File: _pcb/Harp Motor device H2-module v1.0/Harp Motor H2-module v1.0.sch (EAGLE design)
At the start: 52 parts, among them IC1 FT232RL, IC3 LP5907MFX-3.3, IC7 USBLC6-2SC6, IC8 ATXMEGA32A4U, J1 BNCPTH, J2 BNCPTH, J3 POWER_JACK, X1 22-23-2051, X15 Main_plug, X2 22-23-2051, X3 USB_MINI_B, X4 1x4 case, X5 1x3 case, X6 CLCK_JACK, X7 1x4 case, X8 22-23-2021

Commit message: VestibularVR H1BOM updates & Lick Sensor step on
- VestibularVR H1
. component ref updated
. BOM file updated

- Lick Sensor module v1.0
. still only on schematic design
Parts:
- removed J1, J2: BNCPTH, SparkFun-Connectors:BNCPTH
- removed J3: POWER_JACK, SparkFun-Connectors:POWER_JACK
- removed X15: Main_plug, con-weidmueller-sl35:90G-5
- removed X5: 1x3 case, con-molex:22-23-2031
- removed X8: 22-23-2021, con-molex:22-23-2021
- added C1, C14, C15, C16, C17: 100nF, rcl:C-EUC0402K
- added C23, C24: 4.7uF, rcl:C-EUC0603
- added CLKIN: CLCK_JACK, harp input expander:STEREO_JACK
- added HARP: Harp_Intrfc, con-weidmueller-sl35:90G-5
- added IC2, IC4, IC5: 74VHC1GT126DT1G, VestibularVR H1-module v1.0:74LVC1G07DBV
- added IC9: TLV70033DDCR, harp input expander:TLV700XX
- added R1: 330R, rcl:R-US_R0402
- added R11: DNI, rcl:R-US_R0402
- added R12, R13, R2, R4, R6, R7, R8: 10k, rcl:R-US_R0402
- added R5: 10R, rcl:R-US_R0402
- added R9: 1M, rcl:R-US_R0402
- added T1, T2, T3: DMG1012UW??, VestibularVR H1-module v1.0:DMG1012UW-7
- R10: value 330R -> 0R; device rcl:R-EU_R0402 -> rcl:R-US_R0402; MPN RC0402FR-07330RL -> RC0402JR-070RL; OEPS OEPS020037 -> OEPS020001
- R18, R34: DIGIKEY_PN 541-3959-1-ND -> 541-10.0KLDKR-ND
- X1: value 22-23-2051 -> USB_MINI_B; device con-molex:22-23-2051 -> VestibularVR H1-module v1.0:USB_MINI_B; MPN (none) -> UX60-MB-5S8; OEPS (none) -> OEPS070021
- X2: value 22-23-2051 -> Rot_Encoder
- X3: value USB_MINI_B -> EMRG_BUTT_IN_NO; device VestibularVR H1-module v1.0:USB_MINI_B -> con-molex:22-23-2021; MPN UX60-MB-5S8 -> (none); OEPS OEPS070021 -> (none)
- X4: value 1x4 case -> Hall_Effect; device con-molex:22-23-2041 -> con-molex:22-23-2031; MPN 282834-4 Digikey A98335-ND -> 282834-3; OEPS OEPS07 xxx1 -> OEPS070035
- X6: value CLCK_JACK -> BNCPTH; device harp input expander:STEREO_JACK -> SparkFun-Connectors:BNCPTH; MPN 35RASMT2BHNTRX -> (none); NOTES - -> (none); TYPE SMD -> (none)
- X7: value 1x4 case -> STEP_MOTOR; device con-molex:22-23-2041 -> con-molex:22-23-2051; MF - -> (none); MPN 282834-4 Digikey A98335-ND -> (none); OEPS OEPS07 xxx1 -> (none)
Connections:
- removed net N$4: X1-5.S, X2-5.S, X4-4.S
- new net A_PHASE: IC4.A, X2-3.S
- new net B_PHASE: IC5.A, X2-4.S
- new net CLOCK_IN: CLKIN.4, IC8.PB1/ADC9, R2.1
- new net EMERGENCY_INPUT: IC8.PB0/ADC8/AREF, R8.1, X3-1.S
- new net HALL_EFFCT_IN: IC2.A, X4-2.S
- new net LICK_PORT_1: R9.2
- new net N$103: CLKIN.1, R2.2, R5.2
- new net N$104: C24.1, IC9.OUT, R5.1
- new net N$5: C1.1, IC2.VCC, R10.2, R11.2, X4-3.S
- new net STEP_DIRECTION: T1.D, X7-3.S
- new net STEP_ENABLE: T2.D, X7-4.S
- new net STEP_PULSE: T3.D, X7-2.S
- new net U_A_PHASE: IC4.Y, IC8.PC4/OC1A/!SS
- new net U_B_PHASE: IC5.Y, IC8.PC3/OC0D/TXD0
- new net U_HALL_EFFCT_IN: IC2.Y, IC8.PA0/ADC0/AREF
- new net U_STEP_DIRECTION: IC8.PC6/MISO/RXD1, R12.2, T1.G
- new net U_STEP_ENABLE: IC8.PC5/OC1B/MOSI/XCK1, R6.2, T2.G
- new net U_STEP_PULSE: IC8.PC7/SCK/TXD1/CLKO/EVO, R13.2, T3.G
- new net V+: R8.2
- net +12V: now also HARP.1; no longer X15.1
- net +3V3: now also R10.1; no longer X5-3.S
- net +5V: now also C14.1, C17.1, C23.1, IC4.VCC, IC5.VCC, IC9.EN, IC9.IN, R11.1, X2-1.S, X7-1.S
- net GND: now also C1.2, C14.2, C15.2, C16.2, C17.2, C23.2, C24.2, CLKIN.5, HARP.5, IC2.GND, IC4.GND, IC5.GND, IC9.GND, R1.1, R12.1, R13.1, R4.1, R6.1, R7.1, R9.1, T1.S, T2.S, T3.S, X1.5, X2-5.S, X3-2.S, X6.GND, X7-5.S; no longer R10.1, X1-1.S, X15.5, X2-1.S, X3.5, X5-1.S, X6.5
- net HARP_H1_CLOCK_IN: now also HARP.4; no longer X1-2.S
- net HARP_H1_RX: now also HARP.3; no longer X1-3.S
- net HARP_H1_TX: now also HARP.2; no longer X1-4.S
- net N$1: now also X1.P$2; no longer X3.P$2
- net N$15: now also X1.P$3; no longer X3.P$3
- net N$2: now also X1.2; no longer X3.2
- net N$3: now also X1.3; no longer X3.3
- net N$9: now also R1.2; no longer R10.2
- net USB_POWER: now also X1.1; no longer X3.1
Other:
- note added: "Emergency Button NO in"
- note added: "H1 Harp interface InOut"
- note added: "Hall Effect sensor in"
- note added: "harp Clock in"
- note added: "in Stage rotation signal BNC plug: (be sure about)"
- note added: "main USB"
- note added: "out step motor control"
- note removed: "5V~24V inputs (??)"
- note removed: "CHECK VOLTAGE LEVEL OUTPUT!!!"
- note removed: "InOut H1 Harp interface"
- note removed: "Main Plug"
- note removed: "in Clock input"
- note removed: "in Emergency Button"
- note removed: "in Hall Effect sensor"
- note removed: "in jumpers to setup/test open or closed loop control??"
- note removed: "in sphere rotation signal"
- note removed: "in stage rotation signal ?? 2 signals??"
- note removed: "level translatioon 5V -> 3V3"
- note removed: "level translatioon 5V~24V -> 3V3"
- note removed: "out step motor driver"
- note removed: "to u; PullDown"
- moved on the sheet: C10, C11, C12, C13, C2, C25, C26, C27, C28, C29, C3, C4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

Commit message: Harp Motor device H2-module v1.0 - Schematic step on
Harp Motor device H2-module v1.0 - Schematic step on
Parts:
- removed C15, C16: 100nF, rcl:C-EUC0402K
- removed HARP: Harp_Intrfc, con-weidmueller-sl35:90G-5
- removed R10: 0R, rcl:R-US_R0402
- removed R11: DNI, rcl:R-US_R0402
- removed R4, R7: 10k, rcl:R-US_R0402
- removed R9: 1M, rcl:R-US_R0402
- added H2_MAIN_PLUG: be sure about plug type, Harp Motor H2-module v1.0:90G-5
- added IC6: 74AHC1G125DBV, Harp Motor H2-module v1.0:74AHC1G125DBV
- added PWR1: DC_JACK2.1MM, harp camera controller:DC_JACK2.1MM
- C1, C12, C13, C14, C17, C2, C25, C26, C27, C28, C29, C3, C4, C5, C6, C7, C9: device rcl:C-EUC0402K -> Harp Motor H2-module v1.0:C-EUC0402K
- C10, C11: device rcl:C-EUC0603K -> Harp Motor H2-module v1.0:C-EUC0603K
- C8: device rcl:C-EUC0603 -> Harp Motor H2-module v1.0:C-EUC0603
- D4: device diode:BAT54 -> Harp Motor H2-module v1.0:BAT54
- L1, L2: device rcl:R-EU_R0603 -> Harp Motor H2-module v1.0:R-EU_R0603
- R1, R12, R13, R18, R2, R3, R34, R5, R6, R8: device rcl:R-US_R0402 -> Harp Motor H2-module v1.0:R-US_R0402
- STATE: device led:LEDCHIP-LED0603 -> Harp Motor H2-module v1.0:LEDCHIP-LED0603
- SV2: device Connector:PINHD-2X3 -> Harp Motor H2-module v1.0:PINHD-2X3
- TP1, TP10, TP11, TP13: device testpad:TPB1,27 -> Harp Motor H2-module v1.0:TPB1,27
- TP4, TP5, TP6, TP8, TP9: device testpad:TPSQTP11R -> Harp Motor H2-module v1.0:TPSQTP11R
- X2, X7: device con-molex:22-23-2051 -> Harp Motor H2-module v1.0:22-23-2051
- X3: device con-molex:22-23-2021 -> Harp Motor H2-module v1.0:22-23-2021
- X4: device con-molex:22-23-2031 -> Harp Motor H2-module v1.0:22-23-2031
- X6: device SparkFun-Connectors:BNCPTH -> Harp Motor H2-module v1.0:BNCPTH
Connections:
- net A_PHASE renamed ENCODER_A_PHASE
- net B_PHASE renamed ENCODER_B_PHASE
- net U_A_PHASE renamed U_ENCODER_A_PHASE
- net U_B_PHASE renamed U_ENCODER_B_PHASE
- removed net +12V: D4.C, HARP.1
- removed net HARP_H1_CLOCK_IN: HARP.4
- removed net HARP_H1_RX: HARP.3
- removed net HARP_H1_TX: HARP.2
- removed net LICK_PORT_1: R9.2
- removed net N$5: C1.1, IC2.VCC, R10.2, R11.2, X4-3.S
- removed net N$6: D4.A
- new net HARP_H2_CLOCK_IN: H2_MAIN_PLUG.4, IC8.D-/RXD1/MISO/PD6
- new net HARP_H2_RX: H2_MAIN_PLUG.3, IC8.OCB1/XCK1/MOSI/PD5
- new net HARP_H2_TX: H2_MAIN_PLUG.2, IC8.OC1A/!SS!/PD4
- new net N$4: X7-1.S
- new net VDD: H2_MAIN_PLUG.1, PWR1.1
- net +3V3: now also C1.1, IC2.VCC, X4-2.S; no longer R10.1
- net +5V: no longer R11.1, X7-1.S
- net GND: now also H2_MAIN_PLUG.5, PWR1.2, PWR1.3, X4-3.S; no longer C15.2, C16.2, HARP.5, R4.1, R7.1, R9.1, X4-1.S, X6.GND
- net HALL_EFFCT_IN: now also X4-1.S; no longer X4-2.S
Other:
- note added: "BNCs output: connected to two Teensy DAC Stage rotation signal (be sure about)"
- note added: "Camera Controller - Clock_IN: PC2 H1 tb mesmo pino?? - interrupst (?): PC0 PD0 - analog IN: ?? - camera Strobes (Interrupts?): CAM0: PA0=Strobe & PA1=PullUp CAM1: PD6=PullUp & PD7=Strobe"
- note added: "H2 Harp External Power Input - straight to H1 module"
- note added: "H2 Harp main IO plug"
- note added: "USB"
- note added: "V AREV para 3V3 ?!? e Ain para A1"
- note added: "check ferrite case"
- note added: "check pinout not as in abstarct draw"
- note added: "confirmar encoder A & B phase: OC0A & OC0B"
- note added: "connection to Rotary Joint = H1 module"
- note added: "input Emergency Button NO"
- note added: "input Hall Effect home sensor"
- note added: "input harp Clock"
- note added: "input missing?? Treadmill Motion?? what have to do about it?"
- note added: "input rotary encoder"
- note added: "open drain output!! R pull-up out"
- note added: "output step motor control"
- note added: "pinout order: same as sensor"
- note added: "power rail: - Vcc to stepper drive controller optos - DM542 stepper drive controller Vcc: = 5V~24V >> output voltage here can be 5V - Imax = ???"
- note added: "rail de 5V ???? saida para o micro!!!"
- note added: "sensor: WINGONEER JT0701"
- note added: "use the other buffer with EN pin?? that way both buffers can be used"
- note removed: "Emergency Button NO in"
- note removed: "H1 Harp interface InOut"
- note removed: "Hall Effect sensor in"
- note removed: "harp Clock in"
- note removed: "in Stage rotation signal BNC plug: (be sure about)"
- note removed: "in rotary encoder"
- note removed: "main USB"
- note removed: "out step motor control"
- moved on the sheet: C1, C10, C11, C12, C13, C14, C17, C2, C23, C24, C25, C26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

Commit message: Harp Motor device H2-module v1.0 - design proceeding
Harp Motor device H2-module v1.0 - design proceeding
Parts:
- removed IC2, IC4, IC5: 74VHC1GT126DT1G, VestibularVR H1-module v1.0:74LVC1G07DBV
- removed IC6: 74AHC1G125DBV, Harp Motor H2-module v1.0:74AHC1G125DBV
- removed X6: BNCPTH, Harp Motor H2-module v1.0:BNCPTH
- added IC11, IC12, IC13: 74LVC1G125DBV, Harp Motor H2-module v1.0:74LVC1G125DBV
- added R4: 0R, Harp Motor H2-module v1.0:R-US_R0402
- added R7: 10k, Harp Motor H2-module v1.0:R-US_R0402
- R13: value 10k -> DNI; DIGIKEY_PN 541-10.0KLDKR-ND -> -; MPN CRCW040210K0FKED -> -; OEPS OEPS020030 -> -
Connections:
- removed net N$4: X7-1.S
- removed net V+: R8.2
- new net AREF: IC8.PA0/ADC0/AREF, R4.1, R7.2
- net +3V3: now also C14.1, C17.1, IC11.VCC, IC12.VCC, IC13.VCC; no longer IC2.VCC
- net +3V3_U: now also R4.2, R8.2
- net +5V: now also X7-1.S; no longer C14.1, C17.1, IC4.VCC, IC5.VCC
- net ENCODER_A_PHASE: now also IC11.I; no longer IC4.A
- net ENCODER_B_PHASE: now also IC12.I; no longer IC5.A
- net GND: now also IC11.GND, IC11.OE, IC12.GND, IC12.OE, IC13.GND, IC13.OE, R7.1; no longer IC2.GND, IC4.GND, IC5.GND
- net HALL_EFFCT_IN: now also IC13.I; no longer IC2.A
- net U_ENCODER_A_PHASE: now also IC11.O; no longer IC4.Y
- net U_ENCODER_B_PHASE: now also IC12.O; no longer IC5.Y
- net U_HALL_EFFCT_IN: now also IC13.O, IC8.PA1/ADC1; no longer IC2.Y, IC8.PA0/ADC0/AREF
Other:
- note added: "BNCs output: needed?? connected to two Teensy DAC Stage rotation signal ?? (be sure about) maybe only auxiliary IO.."
- note removed: "BNCs output: connected to two Teensy DAC Stage rotation signal (be sure about)"
- note removed: "V AREV para 3V3 ?!? e Ain para A1"
- note removed: "open drain output!! R pull-up out"
- note removed: "rail de 5V ???? saida para o micro!!!"
- note removed: "use the other buffer with EN pin?? that way both buffers can be used"
- moved on the sheet: C1, C14, C17

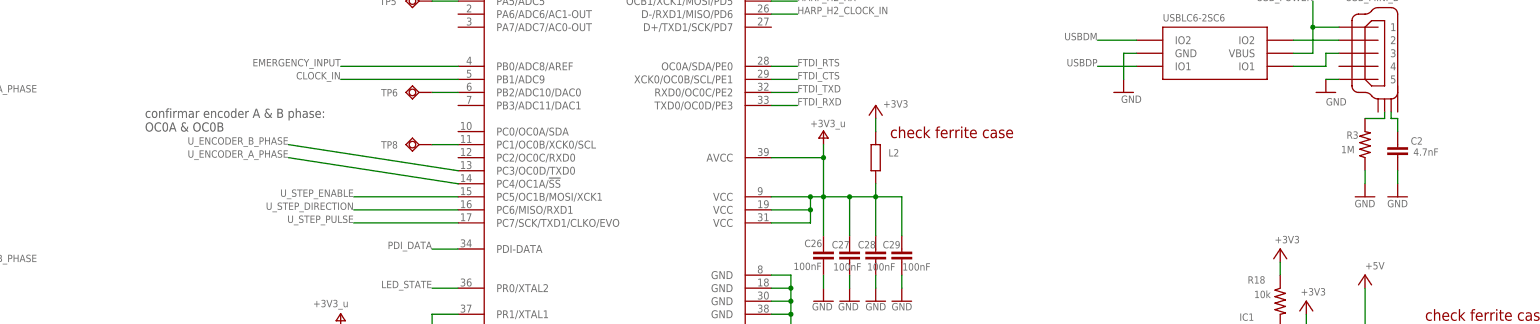
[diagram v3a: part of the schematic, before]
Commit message: Harp Motor device H2-module v1.0 - 1st 'finished' version
Harp Motor device H2-module v1.0 - 1st 'finished' version
- missing:
   . some schm & pcb review with Filipe
   . components order codes & BOM
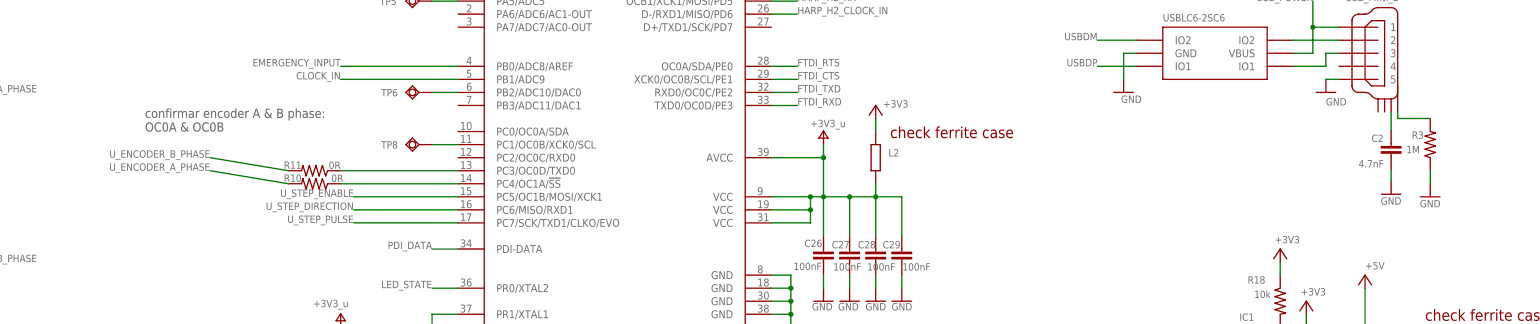
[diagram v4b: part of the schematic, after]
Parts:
- added R10, R11: 0R, Harp Motor H2-module v1.0:R-US_R0402
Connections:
- new net N$59: IC8.PC4/OC1A/!SS, R10.1
- new net N$60: IC8.PC3/OC0D/TXD0, R11.1
- net N$1: now also X1.P$4; no longer X1.P$2
- net U_ENCODER_A_PHASE: now also R10.2; no longer IC8.PC4/OC1A/!SS
- net U_ENCODER_B_PHASE: now also R11.2; no longer IC8.PC3/OC0D/TXD0
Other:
- moved on the sheet: C2, R3
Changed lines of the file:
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@@
 <attribute name="TYPE" value="SMD"/>
+</part>
+<part name="R10" library="Harp Motor H2-module v1.0" deviceset="R-US_" device="R0402" value="0R">
+<attribute name="DIGIKEY_PN" value="o 0R"/>
+<attribute name="MPN" value="MPN ??"/>
+<attribute name="OEPS" value="OEPS?? q codigo"/>
+</part>
+<part name="R11" library="Harp Motor H2-module v1.0" deviceset="R-US_" device="R0402" value="0R">
+<attribute name="DIGIKEY_PN" value="o 0R"/>
+<attribute name="MPN" value="MPN ??"/>
+<attribute name="OEPS" value="OEPS?? q codigo"/>
 </part>
 </parts>
@@
 <attribute name="OEPS" x="358.14" y="101.6" size="1.778" layer="96" rot="MR180" display="off"/>
 </instance>
-<instance part="C2" gate="G$1" x="358.14" y="139.7" smashed="yes">
-<attribute name="NAME" x="360.68" y="139.7" size="1.4224" layer="95" font="vector" ratio="12"/>
-<attribute name="VALUE" x="361.188" y="137.541" size="1.4224" layer="96" font="vector" ratio="12"/>
-<attribute name="MPN" x="358.14" y="139.7" size="1.778" layer="96" display="off"/>
-<attribute name="OEPS" x="358.14" y="139.7" size="1.778" layer="96" display="off"/>
+<instance part="C2" gate="G$1" x="356.87" y="139.954" smashed="yes">
+<attribute name="NAME" x="353.06" y="140.208" size="1.4224" layer="95" font="vector" ratio="12"/>
+<attribute name="VALUE" x="350.52" y="135.255" size="1.4224" layer="96" font="vector" ratio="12"/>
+<attribute name="MPN" x="356.87" y="139.954" size="1.778" layer="96" display="off"/>
+<attribute name="OEPS" x="356.87" y="139.954" size="1.778" layer="96" display="off"/>
 </instance>
 <instance part="GND33" gate="1" x="345.44" y="71.12" smashed="yes">
@@
 <attribute name="VALUE" x="304.292" y="147.828" size="1.4224" layer="96" font="vector" ratio="12"/>
 </instance>
-<instance part="R3" gate="G$1" x="351.79" y="139.7" smashed="yes" rot="R90">
-<attribute name="NAME" x="350.52" y="142.2654" size="1.4224" layer="95" font="vector" ratio="12" rot="R180"/>
-<attribute name="VALUE" x="349.758" y="139.446" size="1.4224" layer="96" font="vector" ratio="12" rot="R180"/>
-<attribute name="MPN" x="351.79" y="139.7" size="1.778" layer="96" rot="R90" display="off"/>
-<attribute name="OEPS" x="351.79" y="139.7" size="1.778" layer="96" rot="R90" display="off"/>
-<attribute name="DIGIKEY_PN" x="351.79" y="139.7" size="1.778" layer="96" rot="R90" display="off"/>
+<instance part="R3" gate="G$1" x="364.49" y="139.7" smashed="yes" rot="R90">
+<attribute name="NAME" x="363.22" y="142.2654" size="1.4224" layer="95" font="vector" ratio="12" rot="R180"/>
+<attribute name="VALUE" x="362.458" y="139.446" size="1.4224" layer="96" font="vector" ratio="12" rot="R180"/>
+<attribute name="MPN" x="364.49" y="139.7" size="1.778" layer="96" rot="R90" display="off"/>
+<attribute name="OEPS" x="364.49" y="139.7" size="1.778" layer="96" rot="R90" display="off"/>
+<attribute name="DIGIKEY_PN" x="364.49" y="139.7" size="1.778" layer="96" rot="R90" display="off"/>
 </instance>
 <instance part="OSC1" gate="G$1" x="165.1" y="93.98" smashed="yes">
@@
 <attribute name="VALUE" x="336.804" y="239.776" size="1.778" layer="96" rot="R180"/>
 </instance>
-<instance part="GND6" gate="1" x="358.14" y="129.54" smashed="yes">
-<attribute name="VALUE" x="356.108" y="127.508" size="1.4224" layer="96" font="vector" ratio="12"/>
-</instance>
-<instance part="GND2" gate="1" x="351.79" y="129.54" smashed="yes">
-<attribute name="VALUE" x="349.758" y="127.508" size="1.4224" layer="96" font="vector" ratio="12"/>
+<instance part="GND6" gate="1" x="356.87" y="130.048" smashed="yes">
+<attribute name="VALUE" x="354.838" y="128.016" size="1.4224" layer="96" font="vector" ratio="12"/>
+</instance>
+<instance part="GND2" gate="1" x="364.49" y="129.54" smashed="yes">
+<attribute name="VALUE" x="362.458" y="127.508" size="1.4224" layer="96" font="vector" ratio="12"/>
 </instance>
 <instance part="GND9" gate="1" x="345.44" y="223.52" smashed="yes">
@@
 <attribute name="OEPS" x="340.36" y="93.98" size="1.778" layer="96" display="off"/>
 <attribute name="OEPS" x="340.36" y="93.98" size="1.778" layer="96" display="off"/>
+</instance>
+<instance part="R10" gate="G$1" x="147.32" y="132.08" smashed="yes" rot="R180">
+<attribute name="NAME" x="144.78" y="133.8834" size="1.4224" layer="95" font="vector" ratio="12" rot="R180"/>
+<attribute name="VALUE" x="152.908" y="133.858" size="1.4224" layer="96" font="vector" ratio="12" rot="R180"/>
+<attribute name="MPN" x="147.32" y="132.08" size="1.778" layer="96" rot="R180" display="off"/>
+<attribute name="DIGIKEY_PN" x="147.32" y="132.08" size="1.778" layer="96" rot="R180" display="off"/>
+<attribute name="OEPS" x="147.32" y="132.08" size="1.778" layer="96" rot="R180" display="off"/>
+</instance>
+<instance part="R11" gate="G$1" x="147.32" y="134.62" smashed="yes" rot="R180">
+<attribute name="NAME" x="144.78" y="136.4234" size="1.4224" layer="95" font="vector" ratio="12" rot="R180"/>
+<attribute name="VALUE" x="152.4" y="136.398" size="1.4224" layer="96" font="vector" ratio="12" rot="R180"/>
+<attribute name="MPN" x="147.32" y="134.62" size="1.778" layer="96" rot="R180" display="off"/>
+<attribute name="DIGIKEY_PN" x="147.32" y="134.62" size="1.778" layer="96" rot="R180" display="off"/>
+<attribute name="OEPS" x="147.32" y="134.62" size="1.778" layer="96" rot="R180" display="off"/>
 </instance>
 </instances>
@@
 <pinref part="C2" gate="G$1" pin="2"/>
 <pinref part="GND6" gate="1" pin="GND"/>
-<wire x1="358.14" y1="132.08" x2="358.14" y2="134.62" width="0.1524" layer="91"/>
+<wire x1="356.87" y1="132.588" x2="356.87" y2="134.874" width="0.1524" layer="91"/>
 </segment>
 <segment>
 <pinref part="GND2" gate="1" pin="GND"/>
 <pinref part="R3" gate="G$1" pin="1"/>
-<wire x1="351.79" y1="132.08" x2="351.79" y2="134.62" width="0.1524" layer="91"/>
+<wire x1="364.49" y1="132.08" x2="364.49" y2="134.62" width="0.1524" layer="91"/>
 </segment>
 <segment>
@@
 <segment>
 <pinref part="R3" gate="G$1" pin="2"/>
-<pinref part="X1" gate="G$1" pin="P$2"/>
-<wire x1="351.79" y1="144.78" x2="355.6" y2="144.78" width="0.1524" layer="91"/>
-<wire x1="355.6" y1="144.78" x2="355.6" y2="146.05" width="0.1524" layer="91"/>
+<wire x1="359.41" y1="144.78" x2="360.68" y2="144.78" width="0.1524" layer="91"/>
+<pinref part="X1" gate="G$1" pin="P$4"/>
+<wire x1="360.68" y1="144.78" x2="364.49" y2="144.78" width="0.1524" layer="91"/>
+<wire x1="358.14" y1="146.05" x2="358.14" y2="144.78" width="0.1524" layer="91"/>
+<wire x1="358.14" y1="144.78" x2="359.41" y2="144.78" width="0.1524" layer="91"/>
 </segment>
 </net>
@@
 <segment>
 <pinref part="X1" gate="G$1" pin="P$3"/>
-<wire x1="356.87" y1="146.05" x2="356.87" y2="144.78" width="0.1524" layer="91"/>
-<wire x1="356.87" y1="144.78" x2="358.14" y2="144.78" width="0.1524" layer="91"/>
+<wire x1="356.87" y1="146.05" x2="356.87" y2="142.494" width="0.1524" layer="91"/>
 <pinref part="C2" gate="G$1" pin="1"/>
-<wire x1="358.14" y1="144.78" x2="358.14" y2="142.24" width="0.1524" layer="91"/>
 </segment>
 </net>
@@
 </segment>
 <segment>
-<label x="142.24" y="139.7" size="1.4224" layer="95" font="vector" ratio="12" rot="MR0"/>
-<pinref part="IC8" gate="G$1" pin="PC3/OC0D/TXD0"/>
-<wire x1="175.26" y1="134.62" x2="142.24" y2="139.7" width="0.1524" layer="91"/>
+<label x="127" y="137.16" size="1.4224" layer="95" font="vector" ratio="12" rot="MR0"/>
+<wire x1="142.24" y1="134.62" x2="127" y2="137.16" width="0.1524" layer="91"/>
+<pinref part="R11" gate="G$1" pin="2"/>
 </segment>
 </net>
 <net name="U_ENCODER_A_PHASE" class="0">
 <segment>
+<label x="127" y="134.62" size="1.4224" layer="95" font="vector" ratio="12" rot="MR0"/>
+<wire x1="142.24" y1="132.08" x2="127" y2="134.62" width="0.1524" layer="91"/>
+<pinref part="R10" gate="G$1" pin="2"/>
+</segment>
+<segment>
 <label x="73.66" y="149.86" size="1.4224" layer="95" font="vector" ratio="12"/>
+<pinref part="IC11" gate="A" pin="O"/>
 <wire x1="58.42" y1="149.86" x2="73.66" y2="149.86" width="0.1524" layer="91"/>
-<pinref part="IC11" gate="A" pin="O"/>
-</segment>
-<segment>
-<label x="142.24" y="137.16" size="1.4224" layer="95" font="vector" ratio="12" rot="MR0"/>
-<wire x1="175.26" y1="132.08" x2="142.24" y2="137.16" width="0.1524" layer="91"/>
-<pinref part="IC8" gate="G$1" pin="PC4/OC1A/!SS"/>
 </segment>
 </net>
@@
 </segment>
 </net>
+<net name="N$59" class="0">
+<segment>
+<pinref part="R10" gate="G$1" pin="1"/>
+<pinref part="IC8" gate="G$1" pin="PC4/OC1A/!SS"/>
+<wire x1="152.4" y1="132.08" x2="175.26" y2="132.08" width="0.1524" layer="91"/>
+</segment>
+</net>
+<net name="N$60" class="0">
+<segment>
+<pinref part="R11" gate="G$1" pin="1"/>
+<pinref part="IC8" gate="G$1" pin="PC3/OC0D/TXD0"/>
+<wire x1="152.4" y1="134.62" x2="175.26" y2="134.62" width="0.1524" layer="91"/>
+</segment>
+</net>
